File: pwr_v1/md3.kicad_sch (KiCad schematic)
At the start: 17 parts, among them M3 Conn_01x08_Socket

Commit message: Schematic and layout updated
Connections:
- net GNDREF: no longer 3C6.2, 3U1.4 (GND_BK), M3.4 (Pin_4)
- new net GND_BK: 3C6.2, 3U1.4 (GND_BK), M3.4 (Pin_4)
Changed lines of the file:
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@@
-	)
-	(junction
-		(at 202.184 67.31)
-		(diameter 0)
-		(color 0 0 0 0)
 	)
 	(junction
@@
 	)
 	(junction
-		(at 136.144 47.879)
-		(diameter 0)
-		(color 0 0 0 0)
-	)
-	(junction
 		(at 202.184 82.55)
-		(diameter 0)
-		(color 0 0 0 0)
-	)
-	(junction
-		(at 123.444 47.879)
 		(diameter 0)
 		(color 0 0 0 0)
@@
 	(wire
 		(pts
-			(xy 202.184 47.879) (xy 136.144 47.879)
+			(xy 123.444 47.879) (xy 123.444 54.61)
 		)
 		(stroke
@@
 	(wire
 		(pts
-			(xy 123.444 47.879) (xy 123.444 54.61)
-		)
-		(stroke
-			(width 0)
-			(type default)
-		)
-	)
-	(wire
-		(pts
 			(xy 145.034 67.31) (xy 145.034 69.85)
 		)
@@
 	(wire
 		(pts
-			(xy 118.11 47.879) (xy 123.444 47.879)
-		)
-		(stroke
-			(width 0)
-			(type default)
-		)
-	)
-	(wire
-		(pts
 			(xy 181.864 60.96) (xy 181.864 62.23)
 		)
@@
 	(wire
 		(pts
-			(xy 194.564 90.17) (xy 194.564 91.44)
-		)
-		(stroke
-			(width 0)
-			(type default)
-		)
-	)
-	(wire
-		(pts
 			(xy 183.134 82.55) (xy 185.674 82.55)
 		)
@@
 		(pts
 			(xy 174.244 53.34) (xy 174.244 54.61)
-		)
-		(stroke
-			(width 0)
-			(type default)
-		)
-	)
-	(wire
-		(pts
-			(xy 202.184 47.879) (xy 202.184 67.31)
 		)
 		(stroke
@@
 	(text "AVDD 3.3V/30mA"
 		(exclude_from_sim no)
-		(at 180.213 47.625 0)
+		(at 203.2 67.31 0)
 		(effects
 			(font
@@
 	)
 	(label "AVDD"
-		(at 118.11 47.879 0)
+		(at 123.444 48.006 0)
 		(fields_autoplaced yes)
 		(effects
@@
 					(unit 1)
 				)
-			)
-		)
-	)
-	(symbol
-		(lib_id "power:GNDREF")
-		(at 194.564 91.44 0)
-		(unit 1)
-		(exclude_from_sim no)
-		(in_bom yes)
-		(on_board yes)
-		(dnp no)
-		(property "Reference" "#PWR035"
-			(at 194.564 97.79 0)
-			(effects
-				(font
-					(size 1.27 1.27)
-				)
-				(hide yes)
-			)
-		)
-		(property "Value" "GNDREF"
-			(at 194.564 95.25 0)
-			(effects
-				(font
-					(size 1.27 1.27)
-				)
-				(hide yes)
-			)
-		)
-		(property "Footprint" ""
-			(at 194.564 91.44 0)
-			(effects
-				(font
-					(size 1.27 1.27)
-				)
-				(hide yes)
-			)
-		)
-		(property "Datasheet" ""
-			(at 194.564 91.44 0)
-			(effects
-				(font
-					(size 1.27 1.27)
-				)
-				(hide yes)
-			)
-		)
-		(property "Description" ""
-			(at 194.564 91.44 0)
-			(effects
-				(font
-					(size 1.27 1.27)
-				)
-				(hide yes)
-			)
-		)
-		(pin "1"
-		)
-		(instances
-			(project "pwr_v1"
-				(path "/42eee4f9-ea65-4e89-8296-df9554a24009/b1b7efd1-e3f8-4df7-b8dd-c3686d4c5699"
-					(reference "#PWR035")
-					(unit 1)
-				)

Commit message: Schematic updated
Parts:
- 3C1: footprint Capacitor_SMD:C_0805_2012Metric -> Capacitor_SMD:C_0402_1005Metric
- 3C2, 3C4, 3C6: footprint Capacitor_SMD:C_0603_1608Metric -> Capacitor_SMD:C_0402_1005Metric
- 3R1: footprint Resistor_SMD:R_0603_1608Metric_Pad0.98x0.95mm_HandSolder -> Resistor_SMD:R_0603_1608Metric

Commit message: Sch and Layout updated; Added batt sup ckt, placed and routed all motor drivers.
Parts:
- M3: footprint Connector_PinHeader_2.54mm:PinHeader_1x08_P2.54mm_Vertical_SMD_Pin1Left -> Connector_PinHeader_2.54mm:PinHeader_1x08_P2.54mm_Vertical
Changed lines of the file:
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@@
 			)
 		)
-		(property "Footprint" "Connector_PinHeader_2.54mm:PinHeader_1x08_P2.54mm_Vertical_SMD_Pin1Left"
+		(property "Footprint" "Connector_PinHeader_2.54mm:PinHeader_1x08_P2.54mm_Vertical"
 			(at 252.984 109.22 0)
 			(effects

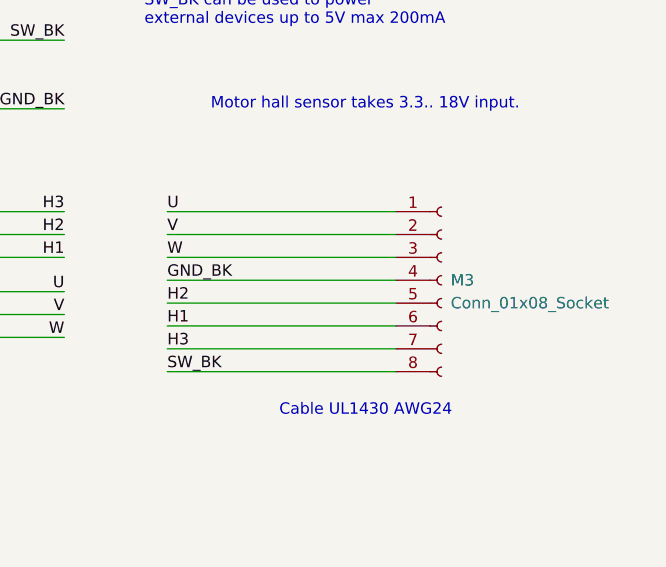
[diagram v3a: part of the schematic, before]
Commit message: Schematic and layout updated; Motor driver alignments and planes;  Few components updated
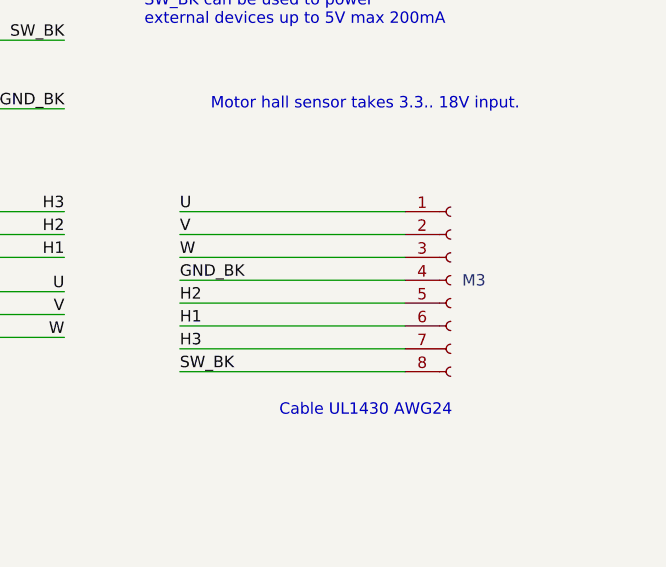
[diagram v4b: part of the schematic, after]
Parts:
- M3: footprint Connector_PinHeader_2.54mm:PinHeader_1x08_P2.54mm_Vertical -> Connector_Molex:Molex_KK-254_AE-6410-08A_1x08_P2.54mm_Vertical
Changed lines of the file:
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@@
 	(wire
 		(pts
-			(xy 222.504 119.38) (xy 247.904 119.38)
+			(xy 223.901 119.38) (xy 248.92 119.38)
 		)
 		(stroke
@@
 	(wire
 		(pts
-			(xy 222.504 111.76) (xy 247.904 111.76)
+			(xy 223.901 111.76) (xy 248.92 111.76)
 		)
 		(stroke
@@
 	(wire
 		(pts
-			(xy 222.504 114.3) (xy 247.904 114.3)
+			(xy 223.901 114.3) (xy 248.92 114.3)
 		)
 		(stroke
@@
 	(wire
 		(pts
-			(xy 222.504 109.22) (xy 247.904 109.22)
+			(xy 223.901 109.22) (xy 248.92 109.22)
 		)
 		(stroke
@@
 	(wire
 		(pts
-			(xy 222.504 104.14) (xy 247.904 104.14)
+			(xy 223.901 104.14) (xy 248.92 104.14)
 		)
 		(stroke
@@
 	(wire
 		(pts
-			(xy 222.504 106.68) (xy 247.904 106.68)
+			(xy 223.901 106.68) (xy 248.92 106.68)
 		)
 		(stroke
@@
 	(wire
 		(pts
-			(xy 222.504 101.6) (xy 247.904 101.6)
+			(xy 223.901 101.6) (xy 248.92 101.6)
 		)
 		(stroke
@@
 	(wire
 		(pts
-			(xy 222.504 116.84) (xy 247.904 116.84)
+			(xy 223.901 116.84) (xy 248.92 116.84)
 		)
 		(stroke
@@
 	)
 	(label "H2"
-		(at 222.504 111.76 0)
+		(at 223.901 111.76 0)
 		(fields_autoplaced yes)
 		(effects
@@
 	)
 	(label "H3"
-		(at 222.504 116.84 0)
+		(at 223.901 116.84 0)
 		(fields_autoplaced yes)
 		(effects
@@
 	)
 	(label "W"
-		(at 222.504 106.68 0)
+		(at 223.901 106.68 0)
 		(fields_autoplaced yes)
 		(effects
@@
 	)
 	(label "U"
-		(at 222.504 101.6 0)
+		(at 223.901 101.6 0)
 		(fields_autoplaced yes)
 		(effects
@@
 	)
 	(label "H1"
-		(at 222.504 114.3 0)
+		(at 223.901 114.3 0)
 		(fields_autoplaced yes)
 		(effects
@@
 	)
 	(label "SW_BK"
-		(at 222.504 119.38 0)
+		(at 223.901 119.38 0)
 		(fields_autoplaced yes)
 		(effects
@@
 	)
 	(label "GND_BK"
-		(at 222.504 109.22 0)
+		(at 223.901 109.22 0)
 		(fields_autoplaced yes)
 		(effects
@@
 	)
 	(label "V"
-		(at 222.504 104.14 0)
+		(at 223.901 104.14 0)
 		(fields_autoplaced yes)
 		(effects
@@
 	)
 	(symbol
+		(lib_id "Connector:Conn_01x08_Socket")
+		(at 254 109.22 0)
+		(unit 1)
+		(exclude_from_sim no)
+		(in_bom yes)
+		(on_board yes)
+		(dnp no)
+		(fields_autoplaced yes)
+		(property "Reference" "M3"
+			(at 255.27 109.2199 0)
+			(effects
+				(font
+					(size 1.27 1.27)
+				)
+				(justify left)
+			)
+		)
+		(property "Value" "Conn_01x08_Socket"
+			(at 255.27 111.7599 0)
+			(effects
+				(font
+					(size 1.27 1.27)
+				)
+				(justify left)
+				(hide yes)
+			)
+		)
+		(property "Footprint" "Connector_Molex:Molex_KK-254_AE-6410-08A_1x08_P2.54mm_Vertical"
+			(at 254 109.22 0)
+			(effects
+				(font
+					(size 1.27 1.27)
+				)
+				(hide yes)
+			)
+		)
+		(property "Datasheet" "~"
+			(at 254 109.22 0)
+			(effects
+				(font
+					(size 1.27 1.27)
+				)
+				(hide yes)
+			)
+		)
+		(property "Description" ""
+			(at 254 109.22 0)
+			(effects
+				(font
+					(size 1.27 1.27)
+				)
+				(hide yes)
+			)
+		)
+		(pin "2"
+		)
+		(pin "7"
+		)
+		(pin "3"
+		)
+		(pin "1"
+		)
+		(pin "8"
+		)
+		(pin "5"
+		)
+		(pin "4"
+		)
+		(pin "6"
+		)
+		(instances
+			(project "pwr_v1"
+				(path "/42eee4f9-ea65-4e89-8296-df9554a24009/b1b7efd1-e3f8-4df7-b8dd-c3686d4c5699"
+					(reference "M3")
+					(unit 1)
+				)
+			)
+		)
+	)
+	(symbol
 		(lib_id "Device:R_Small_US")
 		(at 136.144 57.15 0)
@@
 					(unit 1)
 				)
-			)
-		)
-	)
-	(symbol
-		(lib_id "Connector:Conn_01x08_Socket")
-		(at 252.984 109.22 0)
-		(unit 1)
-		(exclude_from_sim no)
-		(in_bom yes)
-		(on_board yes)
-		(dnp no)
-		(fields_autoplaced yes)
-		(property "Reference" "M3"
-			(at 254 109.2199 0)
-			(effects
-				(font
-					(size 1.27 1.27)
-				)
-				(justify left)
-			)
-		)
-		(property "Value" "Conn_01x08_Socket"
-			(at 254 111.7599 0)
-			(effects
-				(font
-					(size 1.27 1.27)
-				)
-				(justify left)
-			)
-		)
-		(property "Footprint" "Connector_PinHeader_2.54mm:PinHeader_1x08_P2.54mm_Vertical"
-			(at 252.984 109.22 0)
-			(effects
-				(font
-					(size 1.27 1.27)
-				)
-				(hide yes)
-			)
-		)
-		(property "Datasheet" "~"
-			(at 252.984 109.22 0)
-			(effects
-				(font
-					(size 1.27 1.27)
-				)
-				(hide yes)
-			)
-		)
-		(property "Description" "MFR.Part # X6511WVS-08H-C60D48R2 JLCPCB Part # C2883765"
-			(at 252.984 109.22 0)
-			(effects
-				(font
-					(size 1.27 1.27)
-				)
-				(hide yes)
-			)
-		)
-		(pin "2"
-		)
-		(pin "7"
-		)
-		(pin "3"
-		)
-		(pin "1"
-		)
-		(pin "8"
-		)
-		(pin "5"
-		)
-		(pin "4"
-		)
-		(pin "6"
-		)
-		(instances
-			(project "pwr_v1"
-				(path "/42eee4f9-ea65-4e89-8296-df9554a24009/b1b7efd1-e3f8-4df7-b8dd-c3686d4c5699"
-					(reference "M3")
-					(unit 1)
-				)

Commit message: Schematic and layout updated; Layout placement and routing completed
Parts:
- M3: footprint Connector_Molex:Molex_KK-254_AE-6410-08A_1x08_P2.54mm_Vertical -> Connector_PinHeader_2.54mm:PinHeader_1x08_P2.54mm_Vertical
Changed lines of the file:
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@@
 			)
 		)
-		(property "Footprint" "Connector_Molex:Molex_KK-254_AE-6410-08A_1x08_P2.54mm_Vertical"
+		(property "Footprint" "Connector_PinHeader_2.54mm:PinHeader_1x08_P2.54mm_Vertical"
 			(at 254 109.22 0)
 			(effects

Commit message: Sch: 0ohm res added to SPI pins, MD footprints updated; Lay: Silkscreen aligned, logo added, DRC
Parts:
- 3U1: footprint MTR:RGF0040E-IPC_B -> motorDriver:RGF0040E-IPC_B
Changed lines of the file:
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@@
 			)
 		)
-		(property "Footprint" "MTR:RGF0040E-IPC_B"
+		(property "Footprint" "motorDriver:RGF0040E-IPC_B"
 			(at 225.044 59.69 0)
 			(effects

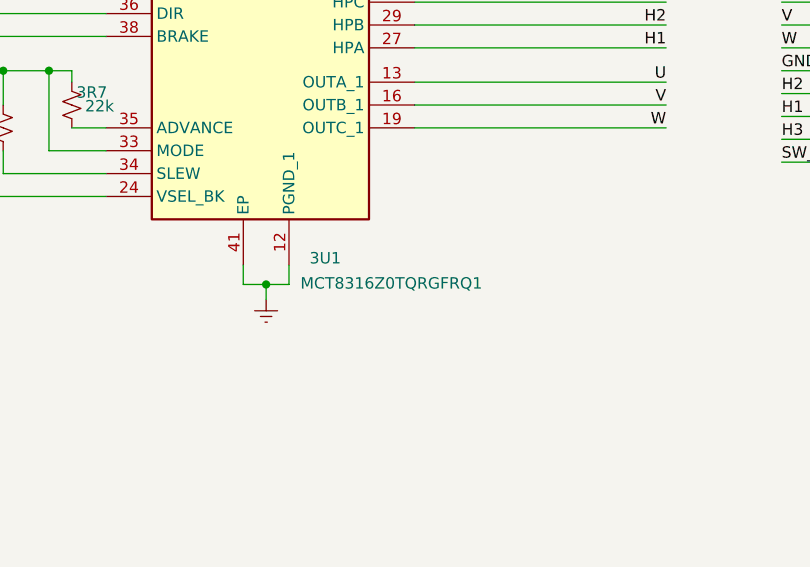
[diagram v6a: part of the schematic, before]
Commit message: Sch: DNP updated, JLC part numbers updated for all components; Lay: Fiducial placement, routing aligned.
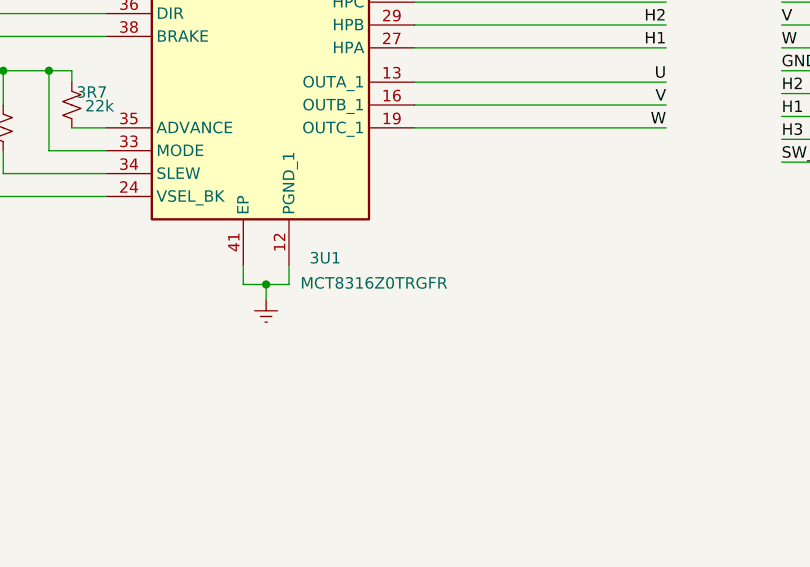
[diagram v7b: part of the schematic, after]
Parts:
- 3U1: value MCT8316Z0TQRGFRQ1 -> MCT8316Z0TRGFR
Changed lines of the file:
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@@
 			)
 		)
-		(property "Description" ""
+		(property "Description" "MFR.Part # HB-PH3-25418PB2GOP JLCPCB Part # C6332201"
 			(at 254 109.22 0)
 			(effects
@@
 			)
 		)
-		(property "Description" "Resistor, small US symbol"
+		(property "Description" "MFR.Part # 0603WAF2702T5E JLCPCB Part # C22967"
 			(at 136.144 57.15 0)
 			(effects
@@
 			)
 		)
-		(property "Value" "MCT8316Z0TQRGFRQ1"
+		(property "Value" "MCT8316Z0TRGFR"
 			(at 170.434 132.842 0)
 			(effects
@@
 			)
 		)
-		(property "Description" ""
+		(property "Description" "MFR.Part # MCT8316Z0TRGFR JLCPCB Part # C3681342"
 			(at 148.844 72.39 0)
 			(effects
@@
 			)
 		)
-		(property "Description" "Resistor, small US symbol"
+		(property "Description" "MFR.Part # 0402WGJ0223TCE JLCPCB Part # C25547"
 			(at 145.034 113.03 0)
 			(effects
@@
 			)
 		)
-		(property "Description" "Resistor, small US symbol"
+		(property "Description" "MFR.Part # RC0805FR-071ML JLCPCB Part # C107700"
 			(at 131.064 115.57 0)
 			(effects
@@
 			)
 		)
-		(property "Description" "Resistor, small US symbol"
+		(property "Description" "MFR.Part # 0603WAF2002T5E JLCPCB Part # C4184"
 			(at 136.144 71.12 0)
 			(effects
@@
 			)
 		)
-		(property "Description" "Resistor, small US symbol"
+		(property "Description" "MFR.Part # 0402WGF4702TCE JLCPCB Part # C25792"
 			(at 137.414 115.57 0)
 			(effects

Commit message: Final PCB files sent for fab
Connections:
- net GNDREF renamed GND
